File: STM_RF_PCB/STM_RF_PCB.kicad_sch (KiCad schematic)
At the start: 46 parts, among them J1 SMA, J2 USB_B_Micro, J3 SWD STLINk, J4 Conn_01x04, SW1 UP, SW2 LF, SW3 DN, SW4 RT, SW5 A, SW6 B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

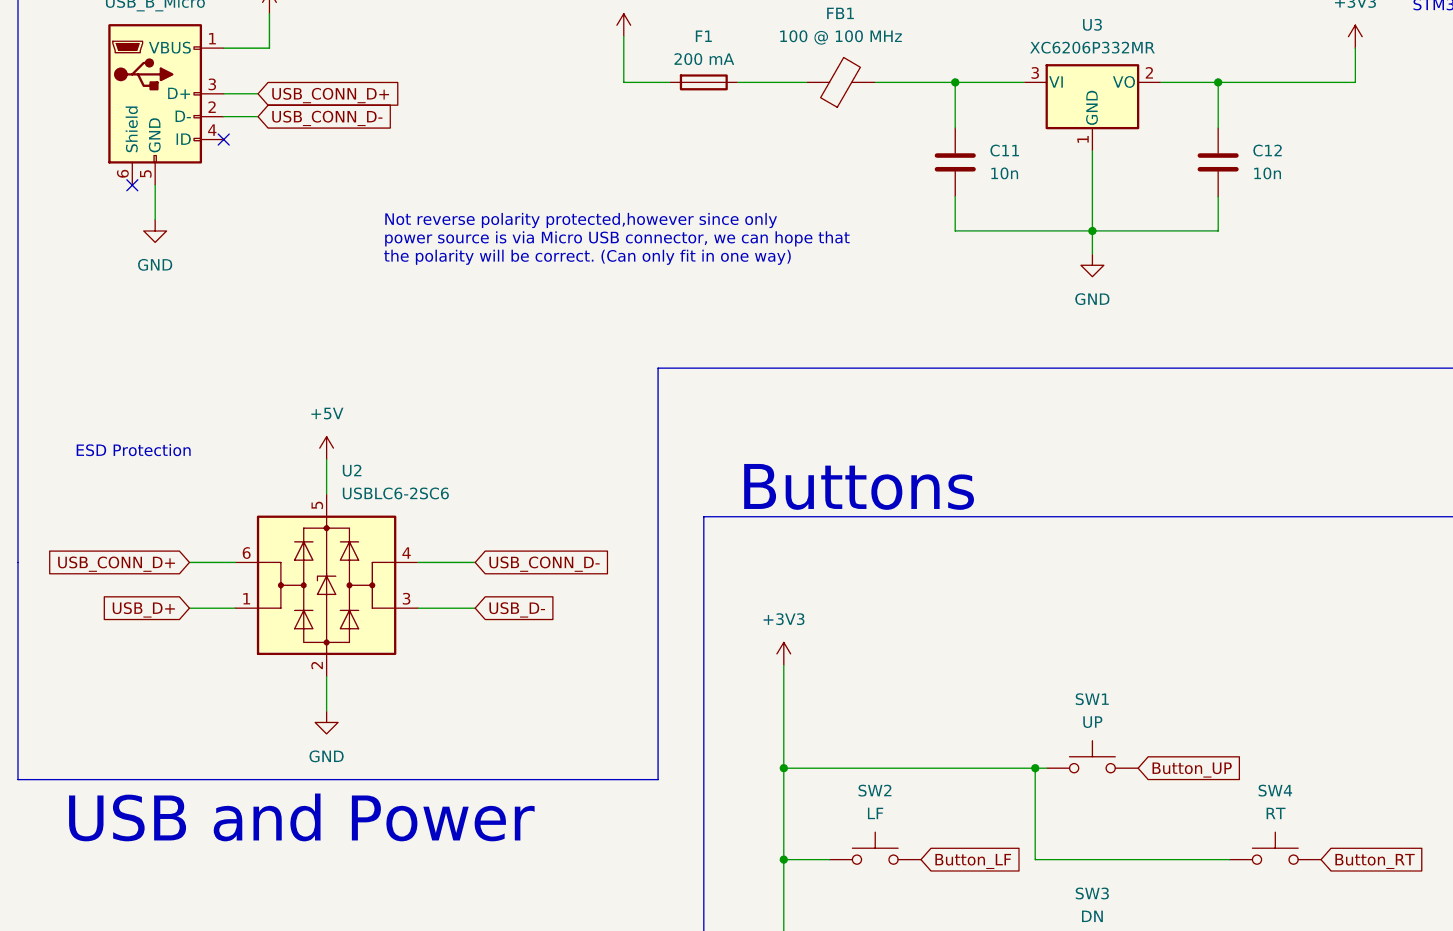
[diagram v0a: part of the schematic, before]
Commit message: Schematic Symbols update for KiCad 8.0, updated footprint for Micro USB, added 3d model to footprint
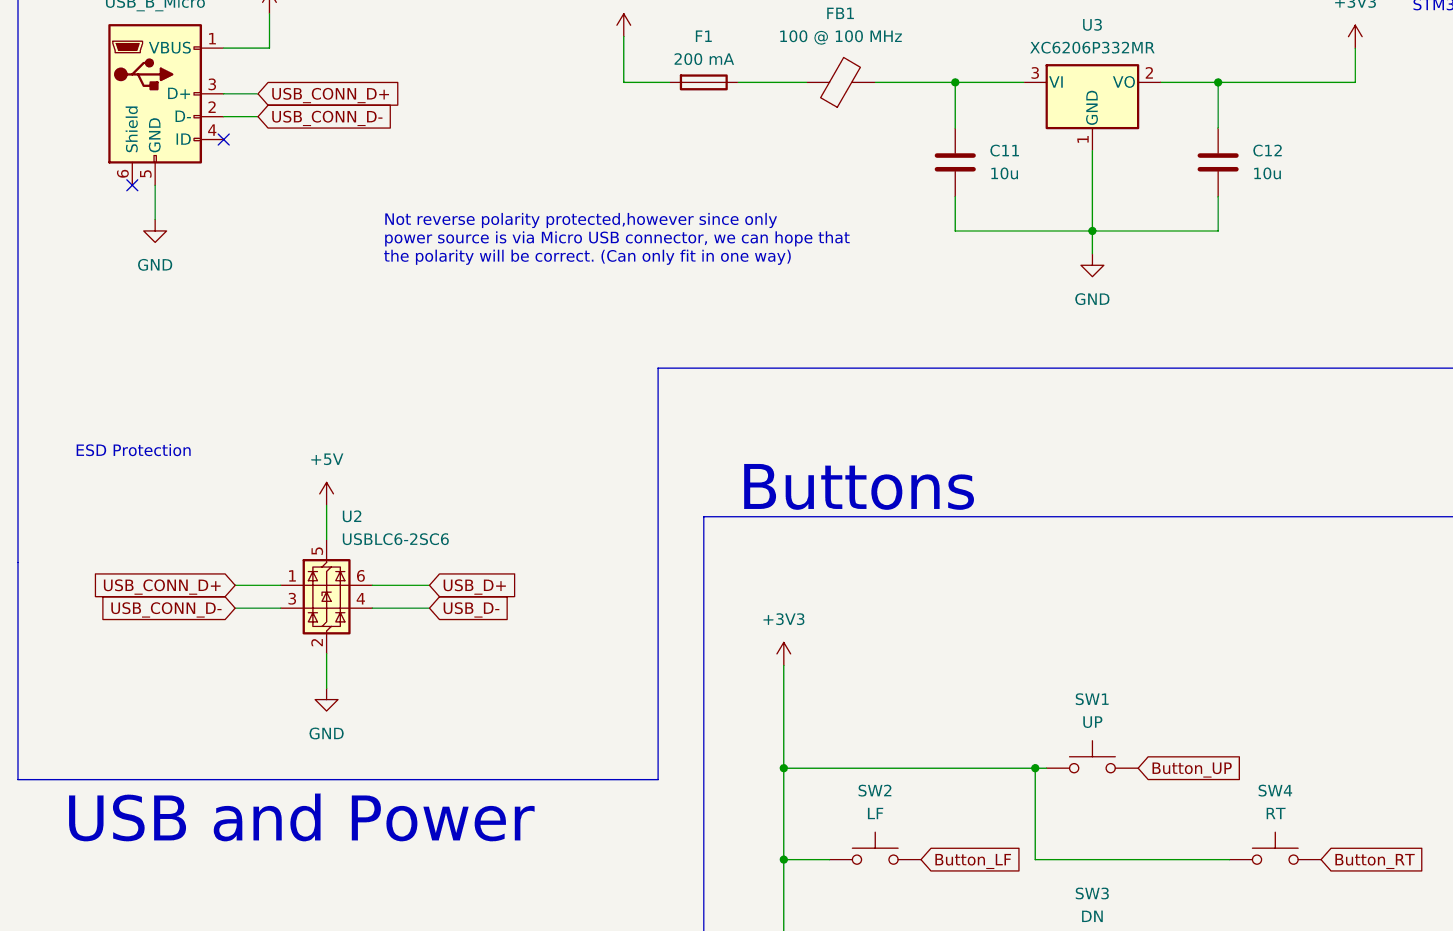
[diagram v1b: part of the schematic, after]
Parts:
- C11, C12: value 10n -> 10u
- J2: footprint (none) -> Library:MICRO-02-G2P3-A1T2
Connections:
- net USB_CONN_D+: now also U2.1 (I/O1); no longer U2.6 (I/O1)
- net USB_CONN_D-: now also U2.3 (I/O2); no longer U2.4 (I/O2)
- net USB_D+: now also U2.6 (I/O1); no longer U2.1 (I/O1)
- net USB_D-: now also U2.4 (I/O2); no longer U2.3 (I/O2)

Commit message: Added part IDs, footprints for all in Power Management
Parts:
- C11, C12: footprint (none) -> Capacitor_SMD:C_0603_1608Metric; Part ID (none) -> CL10A106KP8NNNC
- F1: value 200 mA -> 120 mA; footprint (none) -> Fuse:Fuse_1206_3216Metric; Part ID (none) -> nSMD012
- FB1: footprint (none) -> Inductor_SMD:L_0805_2012Metric; Part ID (none) -> GZ2012D101TF
- J2: Part ID (none) -> MICRO-02-G2P3-A1T2
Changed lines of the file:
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@@
 			)
 		)
-		(property "Footprint" ""
+		(property "Footprint" "Inductor_SMD:L_0805_2012Metric"
 			(at 104.14 37.338 90)
 			(effects
@@
 			)
 		)
+		(property "Part ID" "GZ2012D101TF"
+			(at 104.14 35.56 90)
+			(effects
+				(font
+					(size 1.27 1.27)
+				)
+				(hide yes)
+			)
+		)
 		(pin "1"
 		)
@@
 			)
 		)
-		(property "Footprint" ""
+		(property "Footprint" "Capacitor_SMD:C_0603_1608Metric"
 			(at 147.0152 48.26 0)
 			(effects
@@
 			)
 		)
+		(property "Part ID" "CL10A106KP8NNNC"
+			(at 146.05 44.45 0)
+			(effects
+				(font
+					(size 1.27 1.27)
+				)
+				(hide yes)
+			)
+		)
 		(pin "2"
 		)
@@
 			)
 		)
-		(property "Value" "200 mA"
+		(property "Value" "120 mA"
 			(at 88.9 33.02 90)
 			(effects
@@
 			)
 		)
-		(property "Footprint" ""
+		(property "Footprint" "Fuse:Fuse_1206_3216Metric"
 			(at 88.9 33.782 90)
 			(effects
@@
 			)
 		)
+		(property "Part ID" "nSMD012"
+			(at 88.9 35.56 90)
+			(effects
+				(font
+					(size 1.27 1.27)
+				)
+				(hide yes)
+			)
+		)
 		(pin "1"
 		)
@@
 			)
 		)
-		(property "Footprint" ""
+		(property "Footprint" "Capacitor_SMD:C_0603_1608Metric"
 			(at 117.8052 48.26 0)
 			(effects
@@
 			)
 		)
+		(property "Part ID" "CL10A106KP8NNNC"
+			(at 116.84 44.45 0)
+			(effects
+				(font
+					(size 1.27 1.27)
+				)
+				(hide yes)
+			)
+		)
 		(pin "2"
 		)
@@
 			(at 27.94 36.83 0)
 			(effects
+				(font
+					(size 1.27 1.27)
+				)
+				(hide yes)
+			)
+		)
+		(property "Part ID" "MICRO-02-G2P3-A1T2"
+			(at 27.94 36.83 0)
+			(effects

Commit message: Added footprints and Part ID for I2C Screen
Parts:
- J4: footprint (none) -> Connector_PinSocket_2.54mm:PinSocket_1x04_P2.54mm_Vertical; Part ID (none) -> C2718488
- R6, R7: footprint (none) -> Resistor_SMD:R_0603_1608Metric; Part ID (none) -> 0603WAF2201T5E

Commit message: Small fixes
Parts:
- C1: footprint (none) -> Capacitor_SMD:C_0402_1005Metric; Part ID (none) -> 0402F333M500NT
- C10: value 1.5p -> 1p
- C5, C6: value 22p -> 12p
- R1: footprint (none) -> Resistor_SMD:R_0402_1005Metric; Part ID (none) -> 0402WGF2202TCE
- R3: value 22k -> 10k
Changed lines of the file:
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@@
 	)
 	(junction
+		(at 179.07 205.74)
+		(diameter 0)
+		(color 0 0 0 0)
+	)
+	(junction
+		(at 115.57 256.54)
+		(diameter 0)
+		(color 0 0 0 0)
+	)
+	(junction
 		(at 143.51 161.29)
 		(diameter 0)
@@
 	)
 	(junction
-		(at 171.45 205.74)
-		(diameter 0)
-		(color 0 0 0 0)
-	)
-	(junction
 		(at 63.5 166.37)
 		(diameter 0)
@@
 	(wire
 		(pts
-			(xy 105.41 252.73) (xy 105.41 256.54)
+			(xy 115.57 256.54) (xy 115.57 257.81)
 		)
 		(stroke
@@
 	(wire
 		(pts
-			(xy 171.45 205.74) (xy 171.45 208.28)
+			(xy 179.07 205.74) (xy 179.07 208.28)
 		)
 		(stroke
@@
 	(wire
 		(pts
+			(xy 115.57 256.54) (xy 125.73 256.54)
+		)
+		(stroke
+			(width 0)
+			(type default)
+		)
+	)
+	(wire
+		(pts
 			(xy 134.62 186.69) (xy 143.51 186.69)
 		)
@@
 	(wire
 		(pts
+			(xy 179.07 205.74) (xy 171.45 205.74)
+		)
+		(stroke
+			(width 0)
+			(type default)
+		)
+	)
+	(wire
+		(pts
 			(xy 368.3 156.21) (xy 368.3 166.37)
 		)
@@
 	(wire
 		(pts
+			(xy 115.57 256.54) (xy 105.41 256.54)
+		)
+		(stroke
+			(width 0)
+			(type default)
+		)
+	)
+	(wire
+		(pts
 			(xy 182.88 161.29) (xy 190.5 161.29)
 		)
@@
 	(wire
 		(pts
+			(xy 105.41 256.54) (xy 105.41 252.73)
+		)
+		(stroke
+			(width 0)
+			(type default)
+		)
+	)
+	(wire
+		(pts
 			(xy 210.82 166.37) (xy 210.82 176.53)
 		)
@@
 	(wire
 		(pts
-			(xy 186.69 205.74) (xy 171.45 205.74)
+			(xy 186.69 205.74) (xy 179.07 205.74)
 		)
 		(stroke
@@
 	(symbol
 		(lib_id "power:GND")
-		(at 171.45 208.28 0)
+		(at 179.07 208.28 0)
 		(unit 1)
 		(exclude_from_sim no)
@@
 		(fields_autoplaced yes)
 		(property "Reference" "#PWR09"
-			(at 171.45 214.63 0)
+			(at 179.07 214.63 0)
 			(effects
 				(font
@@
 		)
 		(property "Value" "GND"
-			(at 171.45 213.36 0)
+			(at 179.07 213.36 0)
 			(effects
 				(font
@@
 		)
 		(property "Footprint" ""
-			(at 171.45 208.28 0)
+			(at 179.07 208.28 0)
 			(effects
 				(font
@@
 		)
 		(property "Datasheet" ""
-			(at 171.45 208.28 0)
+			(at 179.07 208.28 0)
 			(effects
 				(font
@@
 		)
 		(property "Description" "Power symbol creates a global label with name \"GND\" , ground"
-			(at 171.45 208.28 0)
+			(at 179.07 208.28 0)
 			(effects
 				(font
@@
 			)
 		)
-		(property "Footprint" ""
+		(property "Footprint" "Resistor_SMD:R_0402_1005Metric"
 			(at 31.242 204.47 90)
 			(effects
@@
 			)
 		)
+		(property "Part ID" "0402WGF2202TCE"
+			(at 33.02 204.47 0)
+			(effects
+				(font
+					(size 1.27 1.27)
+				)
+				(hide yes)
+			)
+		)
 		(pin "2"
 		)
@@
 			)
 		)
-		(property "Footprint" ""
+		(property "Footprint" "Capacitor_SMD:C_0402_1005Metric"
 			(at 45.4152 213.36 0)
 			(effects
@@
 			)
 		)
+		(property "Part ID" "0402F333M500NT"
+			(at 44.45 209.55 0)
+			(effects
+				(font
+					(size 1.27 1.27)
+				)
+				(hide yes)
+			)
+		)
 		(pin "2"
 		)
@@
 			)
 		)
-		(property "Value" "22k"
+		(property "Value" "10k"
 			(at 281.94 168.91 0)
 			(effects
@@
 			)
 		)
-		(property "Value" "1.5p"
+		(property "Value" "1p"
 			(at 194.31 168.91 0)
 			(effects
@@
 			)
 		)
-		(property "Value" "22p"
+		(property "Value" "12p"
 			(at 129.54 250.19 0)
 			(effects
@@
 	)
 	(symbol
-		(lib_id "power:GND")
-		(at 125.73 256.54 0)
-		(unit 1)
-		(exclude_from_sim no)
-		(in_bom yes)
-		(on_board yes)
-		(dnp no)
-		(fields_autoplaced yes)
-		(property "Reference" "#PWR08"
-			(at 125.73 262.89 0)
-			(effects
-				(font
-					(size 1.27 1.27)
-				)
-				(hide yes)
-			)
-		)
-		(property "Value" "GND"
-			(at 125.73 261.62 0)
-			(effects
-				(font
-					(size 1.27 1.27)
-				)
-			)
-		)
-		(property "Footprint" ""
-			(at 125.73 256.54 0)
-			(effects
-				(font
-					(size 1.27 1.27)
-				)
-				(hide yes)
-			)
-		)
-		(property "Datasheet" ""
-			(at 125.73 256.54 0)
-			(effects
-				(font
-					(size 1.27 1.27)
-				)
-				(hide yes)
-			)
-		)
-		(property "Description" "Power symbol creates a global label with name \"GND\" , ground"
-			(at 125.73 256.54 0)
-			(effects
-				(font
-					(size 1.27 1.27)
-				)
-				(hide yes)
-			)
-		)
-		(pin "1"
-		)
-		(instances
-			(project "STM_RF_PCB"
-				(path "/d4ad597f-d032-4e81-a375-ce3c44c27662"
-					(reference "#PWR08")
-					(unit 1)
-				)
-			)
-		)
-	)
-	(symbol
 		(lib_id "Device:C")
 		(at 299.72 223.52 0)
@@
 	(symbol
 		(lib_id "power:GND")
-		(at 105.41 256.54 0)
+		(at 115.57 257.81 0)
 		(unit 1)
 		(exclude_from_sim no)
@@
 		(fields_autoplaced yes)
 		(property "Reference" "#PWR07"
-			(at 105.41 262.89 0)
+			(at 115.57 264.16 0)
 			(effects
 				(font
@@
 		)
 		(property "Value" "GND"
-			(at 105.41 261.62 0)
+			(at 115.57 262.89 0)
 			(effects
 				(font
@@
 		)
 		(property "Footprint" ""
-			(at 105.41 256.54 0)
+			(at 115.57 257.81 0)
 			(effects
 				(font
@@
 		)
 		(property "Datasheet" ""
-			(at 105.41 256.54 0)
+			(at 115.57 257.81 0)
 			(effects
 				(font
@@
 		)
 		(property "Description" "Power symbol creates a global label with name \"GND\" , ground"
-			(at 105.41 256.54 0)
+			(at 115.57 257.81 0)
 			(effects
 				(font
@@
 			)
 		)
-		(property "Value" "22p"
+		(property "Value" "12p"
 			(at 109.22 250.19 0)
 			(effects

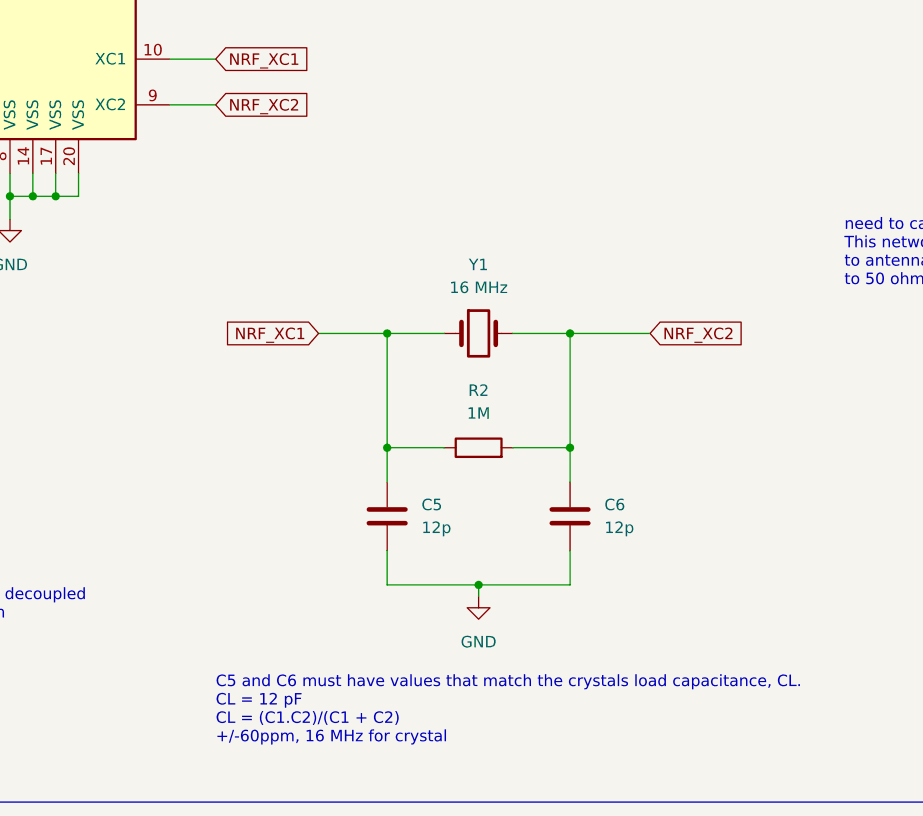
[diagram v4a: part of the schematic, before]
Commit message: Footprints, part ID for RF block except SMA
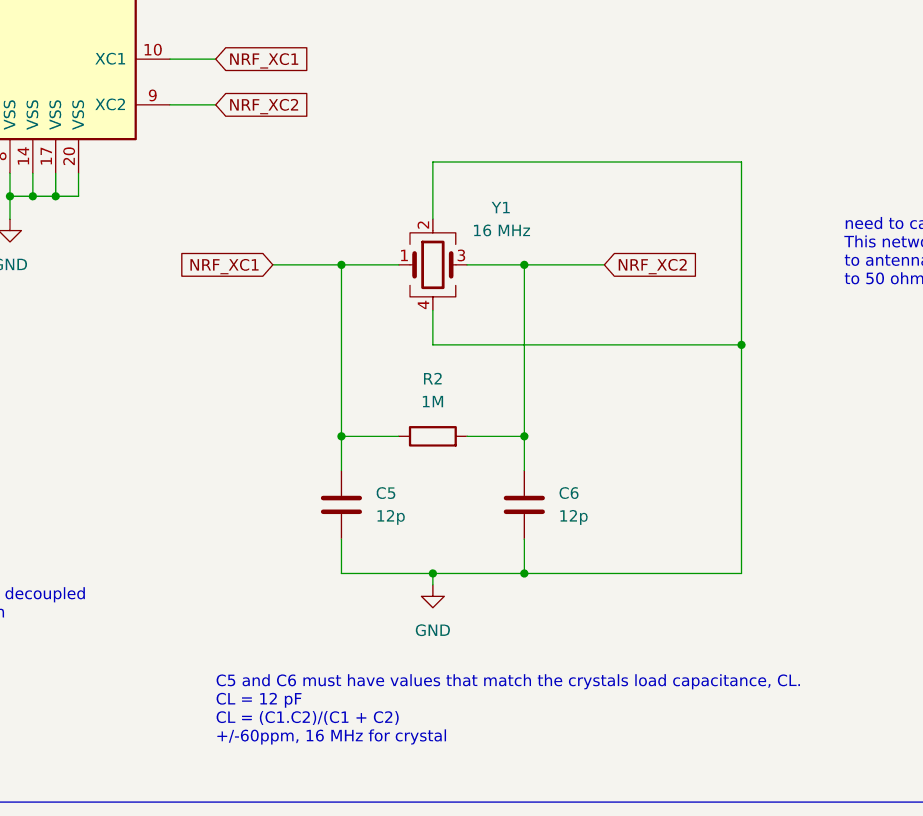
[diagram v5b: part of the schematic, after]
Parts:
- C10: footprint (none) -> Capacitor_SMD:C_0402_1005Metric; Part ID (none) -> 0402CG1R0C500NT
- C2: footprint (none) -> Resistor_SMD:R_0603_1608Metric; Part ID (none) -> CL10A106KP8NNNC
- C3: footprint (none) -> Capacitor_SMD:C_0402_1005Metric; Part ID (none) -> CC0402KRX7R7BB102
- C4: footprint (none) -> Capacitor_SMD:C_0603_1608Metric; Part ID (none) -> CL10A475KP8NNNC
- C5, C6: footprint (none) -> Capacitor_SMD:C_0402_1005Metric; Part ID (none) -> 0402CG120J500NT
- C7: footprint (none) -> Capacitor_SMD:C_0402_1005Metric; Part ID (none) -> 0402B222K500NT
- C8: footprint (none) -> Capacitor_SMD:C_0402_1005Metric; Part ID (none) -> 0402CG4R7C500NT
- C9: footprint (none) -> Capacitor_SMD:C_0402_1005Metric; Part ID (none) -> 0402CG1R5C500NT
- L1: footprint (none) -> Inductor_SMD:L_0402_1005Metric; Part ID (none) -> SDCL1005C2N7STDF
- L2: footprint (none) -> Inductor_SMD:L_0402_1005Metric; Part ID (none) -> SDCL1005C8N2JTDF
- L3: footprint (none) -> Inductor_SMD:L_0402_1005Metric; Part ID (none) -> SDCL1005C3N9STDF
- R2: footprint (none) -> Resistor_SMD:R_0402_1005Metric; Part ID (none) -> 0402WGF1004TCE
- Y1: footprint (none) -> Crystal:Crystal_SMD_3225-4Pin_3.2x2.5mm; symbol Device:Crystal -> Device:Crystal_GND24; Part ID (none) -> X322516MLB4SI
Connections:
- net GND: now also Y1.2, Y1.4
- net NRF_XC2: now also Y1.3; no longer Y1.2
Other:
- moved on the sheet: C5, C6, R2

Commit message: Footprint and Part ID for SMA antenna
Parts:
- J1: footprint (none) -> Library:SMA-KWE902; Part ID (none) -> SMA-KWE902
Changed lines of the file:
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@@
 			)
 		)
-		(property "Footprint" ""
+		(property "Footprint" "Library:SMA-KWE902"
 			(at 210.82 161.29 0)
 			(effects
@@
 			(at 210.82 161.29 0)
 			(effects
+				(font
+					(size 1.27 1.27)
+				)
+				(hide yes)
+			)
+		)
+		(property "Part ID" "SMA-KWE902"
+			(at 210.82 161.29 0)
+			(effects

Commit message: STM32 block footprints, Part IDs
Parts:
- C13, C14, C15, C16: footprint (none) -> Capacitor_SMD:C_0402_1005Metric; Part ID (none) -> CL05B104KO5NNNC
- C17: footprint (none) -> Capacitor_SMD:C_0603_1608Metric; Part ID (none) -> CL10A475KP8NNNC
- D1: footprint (none) -> LED_SMD:LED_0603_1608Metric; Part ID (none) -> 19-213/Y2C-CQ2R2L/3T(CY)
- D2: footprint (none) -> LED_SMD:LED_0603_1608Metric; Part ID (none) -> 19-217/GHC-YN1P2B18X/6T
- J3: footprint (none) -> Connector_PinHeader_2.54mm:PinHeader_2x05_P2.54mm_Vertical; Part ID (none) -> HB-PH8-25425PB2GOP
- R3: footprint (none) -> Resistor_SMD:R_0402_1005Metric; Part ID (none) -> 0402WGF1002TCE
- R4, R5: footprint (none) -> Resistor_SMD:R_0603_1608Metric; Part ID (none) -> 0603WAF2201T5E
- U4: footprint Package_DFN_QFN:QFN-32-1EP_5x5mm_P0.5mm_EP3.45x3.45mm -> Package_DFN_QFN:UFQFPN-32-1EP_5x5mm_P0.5mm_EP3.5x3.5mm; Part ID (none) -> C94784

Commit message: Buttons block, footprint and part ID
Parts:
- SW1, SW2, SW3, SW4, SW5, SW6: footprint (none) -> Library:TC-1103-C-D; Part ID (none) -> TC-1103-C-D
